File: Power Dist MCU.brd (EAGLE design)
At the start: 100 x 80 mm, 10 parts

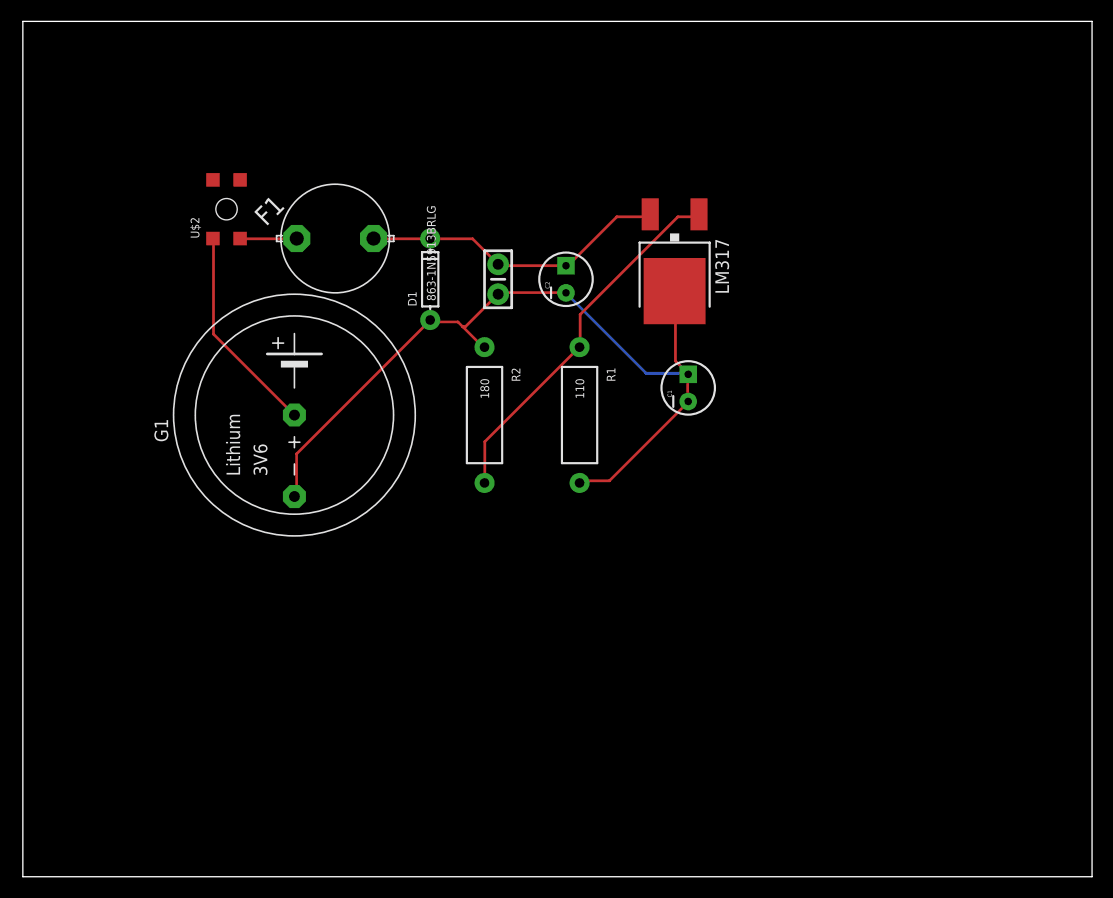
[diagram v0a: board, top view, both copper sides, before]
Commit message: Fixed up the schematics and PCBs for power dist
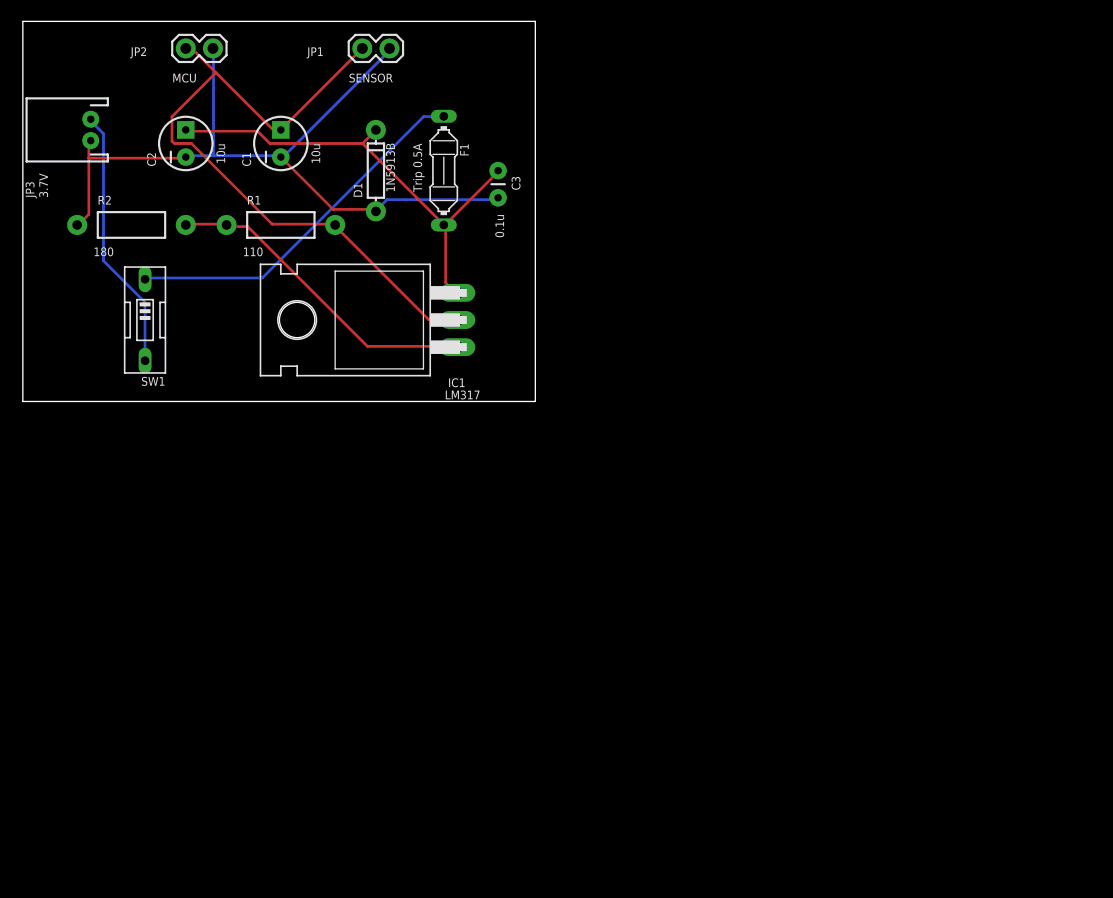
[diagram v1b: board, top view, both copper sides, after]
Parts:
- removed G1: 3.7V, battery:SL-340/P3.6V
- removed LM317: Net 3.3V, SparkFun-PowerIC:V-REG_DPACK
- removed U$2: (no value), GeekAmmo:7914G
- added IC1: LM317, linear:TO220H
- added JP1: SENSOR, SparkFun-Connectors:1X02
- added JP2: MCU, SparkFun-Connectors:1X02
- added JP3: 3.7V, SparkFun-Connectors:JST-2-PTH
- added SW1: (no value), special:EDG-01
- C3: device SparkFun-Capacitors:CAP-PTH-SMALL-KIT -> SparkFun-Capacitors:CAP-PTH-SMALL
- D1: value 863-1N5913BRLG -> 1N5913B
- F1: device fuse:19559 -> fuse:PICOFUSE
- R1, R2: device SparkFun-Resistors:AXIAL-0.5 -> SparkFun-Passives:AXIAL-0.4
- moved C1 44.4 mm to (24.1, 68.6)
- moved C2 37.8 mm to (15.2, 68.6)
- moved R2 37.5 mm to (10.2, 61.0), turned to 0 degrees
- moved R1 33.1 mm to (24.1, 61.0), turned to 0 degrees
- moved F1 12.0 mm to (39.4, 66.0), turned to 270 degrees
- moved D1 11.4 mm to (33.0, 66.0)
- moved C3 10.2 mm to (44.5, 66.0)
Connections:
- removed net N$3: F1.1, U$2.3
- new net N$5: C2.1, C3.1, D1.C, F1.2, IC1.3
- new net VOUT: C1.1, IC1.2, JP1.1, JP2.1, R1.P$2
- net GND: now also C1.2, C2.2, C3.2, D1.A, JP1.2, JP2.2, JP3.1, R2.P$1; no longer C2.1, C3.1, D1.C, F1.2, LM317.3
- net N$1: now also F1.1, SW1.1; no longer C1.1, C1.2, C2.2, C3.2, D1.A, G1.-, LM317.4, R1.P$2, R2.P$1
- net N$2: now also JP3.2, SW1.2; no longer G1.+, U$2.1
- net N$4: now also IC1.1; no longer LM317.1
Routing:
- net VOUT: track 0.00 -> 64.6 mm
- net GND: track 28.9 -> 74.3 mm
- net N$5: track 0.00 -> 43.8 mm
- net N$1: track 77.8 -> 34.3 mm
- net N$3: track 5.32 -> 0.00 mm
- net N$2: track 19.7 -> 24.7 mm
- net N$4: track 34.5 -> 30.2 mm
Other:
- board size 100 x 80 mm -> 47.9 x 35.5 mm
